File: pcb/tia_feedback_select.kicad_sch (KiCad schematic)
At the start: 13 parts, among them U14 TMUX6112, U20 MC74HC238ADTR2G

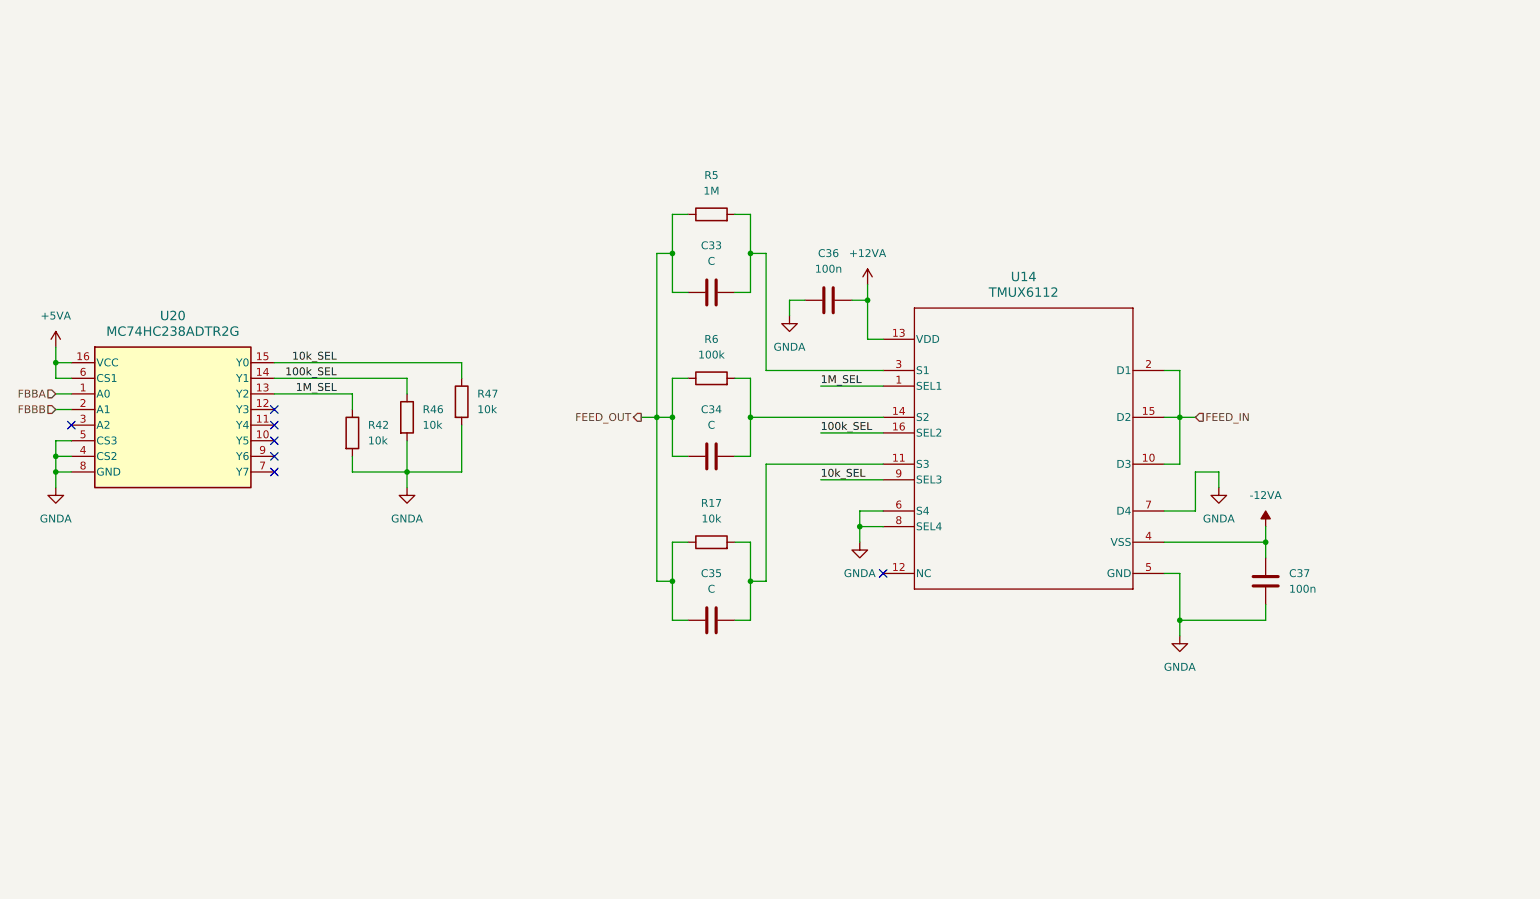
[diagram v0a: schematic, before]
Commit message: reworked the digital isolation block
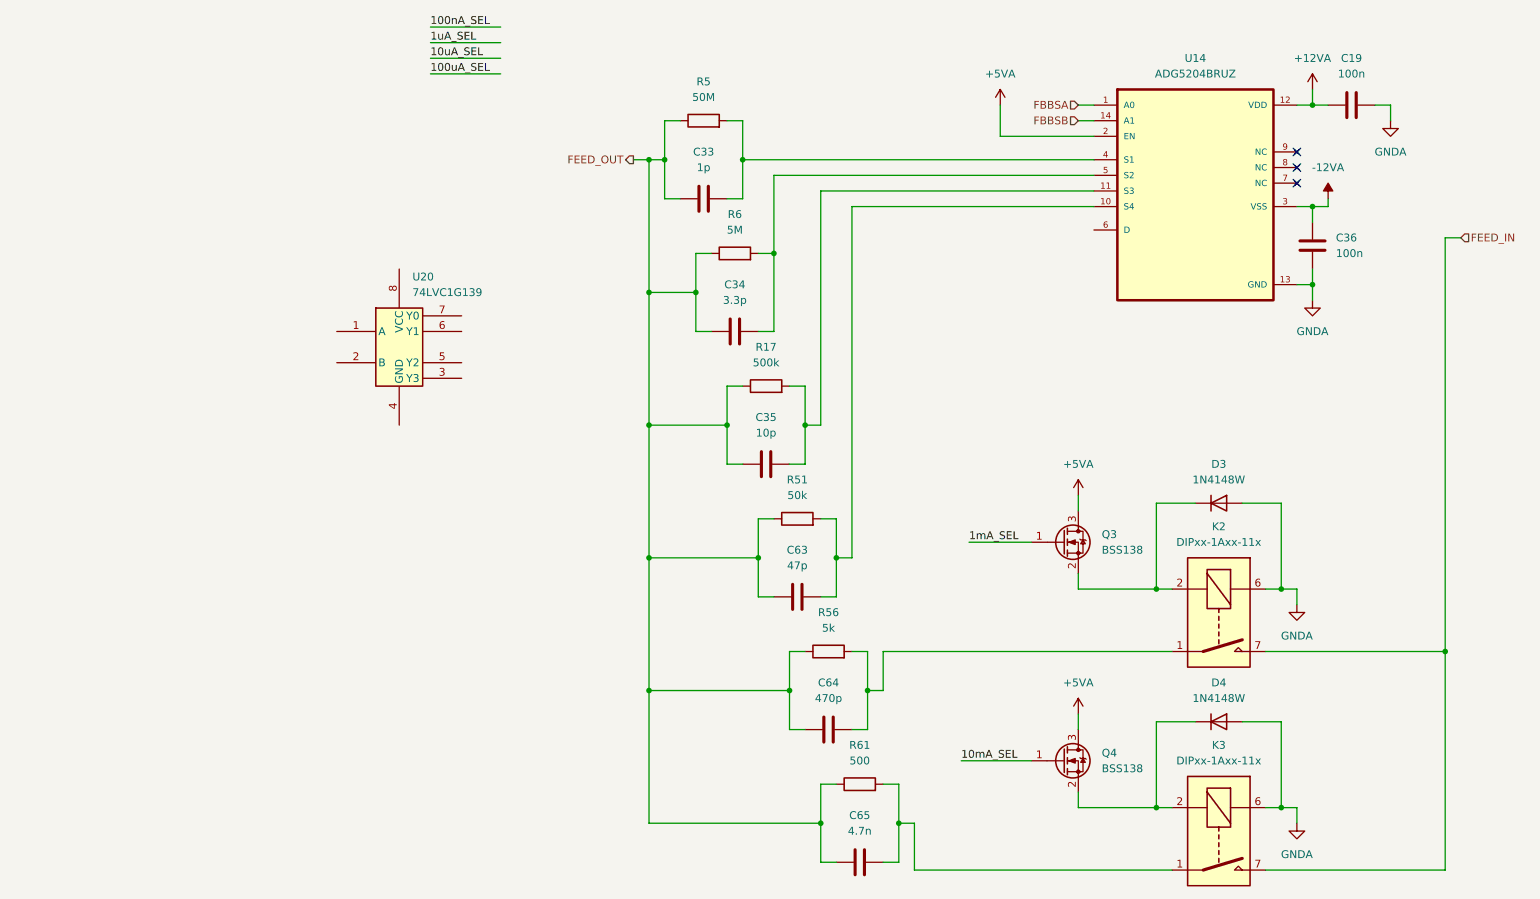
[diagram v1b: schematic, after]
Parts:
- removed C37: 100n, symbol Device:C
- removed R42, R46, R47: 10k, symbol Device:R
- removed U14: TMUX6112, PW0016A_N, symbol project_library:TMUX6112
- removed U20: MC74HC238ADTR2G, TSSOP-16_ONS, symbol project_library:MC74HC238ADTR2G
- added C19: 100n, symbol Device:C
- added C63: 47p, symbol Device:C
- added C64: 470p, symbol Device:C
- added C65: 4.7n, symbol Device:C
- added D3, D4: 1N4148W, Diode_SMD:D_SOD-123, symbol Diode:1N4148W
- added K2, K3: DIPxx-1Axx-11x, Relay_THT:Relay_StandexMeder_DIP_LowProfile, symbol Relay:DIPxx-1Axx-11x
- added Q3, Q4: BSS138, Package_TO_SOT_SMD:SOT-23, symbol Transistor_FET:BSS138
- added R51: 50k, symbol Device:R
- added R56: 5k, symbol Device:R
- added R61: 500, symbol Device:R
- added U14: ADG5204BRUZ, ADG5204BRUZ:SOP65P640X120-14N, symbol project_library:ADG5204BRUZ
- added U20: 74LVC1G139, symbol 74xGxx:74LVC1G139
- C33: value C -> 1p
- C34: value C -> 3.3p
- C35: value C -> 10p
- R17: value 10k -> 500k
- R5: value 1M -> 50M
- R6: value 100k -> 5M
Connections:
- net +12VA: now also C19.2, U14.12 (VDD); no longer C36.2
- net +5VA: now also Q3.3 (D), Q4.3 (D), U14.2 (EN)
- net -12VA: now also C36.2, U14.3 (VSS)
- net FEED_IN: now also K2.7, K2.8, K3.7, K3.8
- net FEED_OUT: now also C63.1, C64.1, C65.1, R51.1, R56.1, R61.1
- net GNDA: now also C19.1, D3.2 (A), D4.2 (A), K2.6, K3.6, U14.13 (GND)
- net at C33.2, R5.2: now also U14.4 (S1)
- net at C34.2, R6.2: now also U14.5 (S2)
- net at C35.2, R17.2: now also U14.11 (S3)
- new net: C63.2, R51.2, U14.10 (S4)
- new net: D3.1 (K), K2.2, Q3.2 (S)
- new net: D4.1 (K), K3.2, Q4.2 (S)
- new net: C65.2, K3.1, K3.14, R61.2
- new net: C64.2, K2.1, K2.14, R56.2
- new net 10mA_SEL: Q4.1 (G)
- new net 1mA_SEL: Q3.1 (G)
- new net FBBSA: U14.1 (A0)
- new net FBBSB: U14.14 (A1)
- no-connect marks 7 -> 3
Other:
- moved on the sheet: C33, C34, C35, C36, R17, R5, R6

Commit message: rework to tia feedback selection, board power, and ui
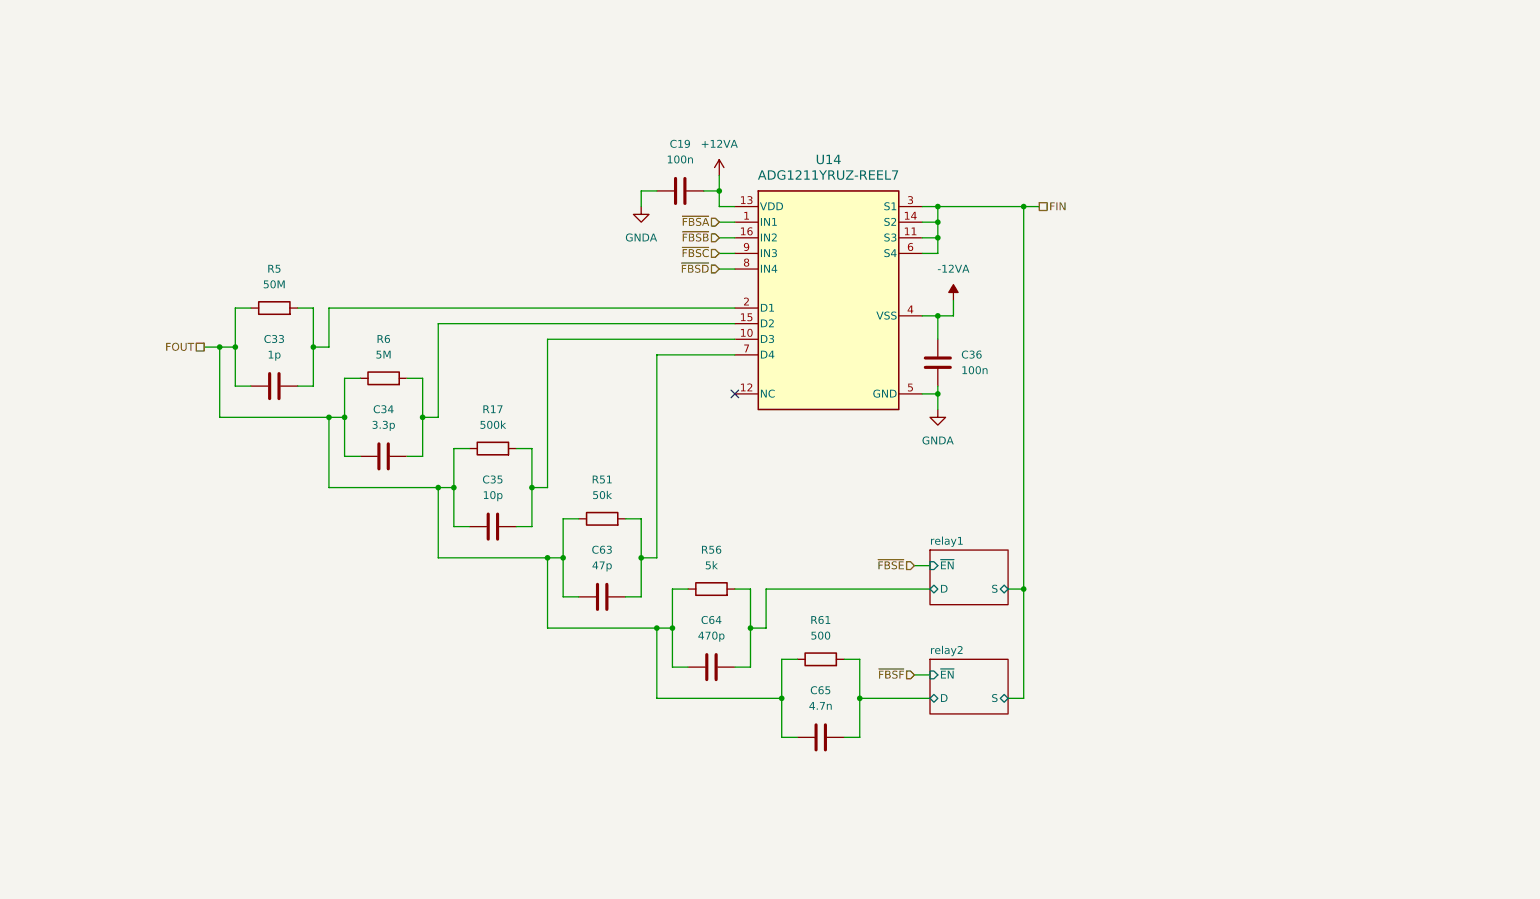
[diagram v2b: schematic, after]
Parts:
- removed D3, D4: 1N4148W, Diode_SMD:D_SOD-123, symbol Diode:1N4148W
- removed K2, K3: DIPxx-1Axx-11x, Relay_THT:Relay_StandexMeder_DIP_LowProfile, symbol Relay:DIPxx-1Axx-11x
- removed Q3, Q4: BSS138, Package_TO_SOT_SMD:SOT-23, symbol Transistor_FET:BSS138
- removed U14: ADG5204BRUZ, ADG5204BRUZ:SOP65P640X120-14N, symbol project_library:ADG5204BRUZ
- removed U20: 74LVC1G139, symbol 74xGxx:74LVC1G139
- added U14: ADG1211YRUZ-REEL7, RU_16_ADI, symbol project_library:ADG1211YRUZ-REEL7
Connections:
- net +12VA: now also C19.1, U14.13 (VDD); no longer C19.2
- net -12VA: now also U14.4 (VSS)
- net GNDA: now also C19.2, U14.5 (GND); no longer C19.1
- net at C33.2, R5.2: now also U14.2 (D1)
- net at C63.2, R51.2: now also U14.7 (D4)
- net relay2/D: now reaches C65.2, R61.2
- net at C34.2, R6.2: now also U14.15 (D2)
- net at C35.2, R17.2: now also U14.10 (D3)
- net relay1/D: now reaches C64.2, R56.2
- net FEED_OUT renamed FOUT
- new net FIN: U14.11 (S3), U14.14 (S2), U14.3 (S1), U14.6 (S4)
- new net ~{FBSA}: U14.1 (IN1)
- new net ~{FBSB}: U14.16 (IN2)
- new net ~{FBSC}: U14.9 (IN3)
- new net ~{FBSD}: U14.8 (IN4)
- no-connect marks 3 -> 1
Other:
- added sheet relay1 (relay.kicad_sch)
- added sheet relay2 (relay.kicad_sch)
- moved on the sheet: C19, C33, C34, C35, C36, C63, C64, C65, R17, R5, R51, R56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
